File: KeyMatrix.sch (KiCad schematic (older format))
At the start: 104 parts, among them SW10 CherryMX, SW11 CherryMX, SW12 CherryMX, SW13 CherryMX, SW14 CherryMX, SW15 CherryMX, SW16 CherryMX, SW17 CherryMX, SW18 CherryMX, SW19 CherryMX, SW2 CherryMX, SW20 CherryMX, SW21 CherryMX, SW22 CherryMX, SW23 CherryMX, SW24 CherryMX, SW25 CherryMX, SW26 CherryMX, SW27 CherryMX, SW28 CherryMX, SW29 CherryMX, SW3 CherryMX, SW30 CherryMX, SW31 CherryMX, SW32 CherryMX, SW33 CherryMX, SW34 CherryMX, SW35 CherryMX, SW36 CherryMX, SW37 CherryMX, SW38 CherryMX, SW39 CherryMX, SW4 CherryMX, SW40 CherryMX, SW41 CherryMX, SW42 CherryMX, SW43 CherryMX, SW44 CherryMX, SW45 CherryMX, SW46 CherryMX, SW47 CherryMX, SW48 CherryMX, SW49 CherryMX, SW5 CherryMX, SW50 CherryMX, SW51 CherryMX, SW52 CherryMX, SW53 CherryMX, SW6 CherryMX, SW7 CherryMX, SW8 CherryMX, SW9 CherryMX

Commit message: Case outline and mounting
Received kprepublic case, used dimensions to set drawing of case and pcb outline. Created M2 screw footprint and added mounting holes to project. Tied screws to power gnd, will possibly change to signal ground later. Changed switches to be kailh hotswaps.
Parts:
- removed D52: D, ortho-40percent:SOD-123, symbol master-vampire_General:D
- removed SW53: CherryMX, CherryMX:SW_Cherry-MX_1U_PCB-Mount, symbol MKB_Switches:CherryMX
- SW10, SW11, SW12, SW13, SW14, SW15, SW16, SW17, SW18, SW19, SW2, SW20, SW21, SW22, SW23, SW24, SW25, SW26, SW27, SW28, SW29, SW3, SW30, SW31, SW32, SW33, SW34, SW35, SW36, SW37, SW38, SW39, SW4, SW40, SW41, SW42, SW43, SW44, SW45, SW46, SW47, SW48, SW49, SW5, SW6, SW7, SW8, SW9: footprint CherryMX:SW_Cherry-MX_1U_PCB-Mount -> CherryMX:SW_Cherry-MX_1U_PCB-Mount_Kailh-Hot-Swap
- SW50, SW51, SW52: footprint CherryMX:SW_Cherry-MX_1U_PCB-Mount -> CherryMX:SW_Cherry-MX_1U_PCB-Mount_Kailh-Hot-Swap; Package 1u -> 2u

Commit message: 2u footprint and plate comments
Finished 2u footprint in all styles. Added cutouts by using Cmts.User layer.
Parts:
- SW50, SW51, SW52: footprint CherryMX:SW_Cherry-MX_1U_PCB-Mount_Kailh-Hot-Swap -> CherryMX:SW_Cherry-MX_2U_PCB-Mount_Kailh-Hot-Swap
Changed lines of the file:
@@
 F 0 "SW50" H 8833 4955 50  0000 C CNN
 F 1 "CherryMX" H 8833 4864 50  0000 C CNN
-F 2 "CherryMX:SW_Cherry-MX_1U_PCB-Mount_Kailh-Hot-Swap" H 9600 4650 50  0001 C CNN
+F 2 "CherryMX:SW_Cherry-MX_2U_PCB-Mount_Kailh-Hot-Swap" H 9600 4650 50  0001 C CNN
 F 3 "" H 9500 4650 50  0001 C CNN
 F 4 "DNP" H 8700 4550 50  0001 C CNN "Manufacturer"
@@
 F 0 "SW51" H 8833 6155 50  0000 C CNN
 F 1 "CherryMX" H 8833 6064 50  0000 C CNN
-F 2 "CherryMX:SW_Cherry-MX_1U_PCB-Mount_Kailh-Hot-Swap" H 9600 5850 50  0001 C CNN
+F 2 "CherryMX:SW_Cherry-MX_2U_PCB-Mount_Kailh-Hot-Swap" H 9600 5850 50  0001 C CNN
 F 3 "" H 9500 5850 50  0001 C CNN
 F 4 "DNP" H 8700 5750 50  0001 C CNN "Manufacturer"
@@
 F 0 "SW52" H 8833 7355 50  0000 C CNN
 F 1 "CherryMX" H 8833 7264 50  0000 C CNN
-F 2 "CherryMX:SW_Cherry-MX_1U_PCB-Mount_Kailh-Hot-Swap" H 9600 7050 50  0001 C CNN
+F 2 "CherryMX:SW_Cherry-MX_2U_PCB-Mount_Kailh-Hot-Swap" H 9600 7050 50  0001 C CNN
 F 3 "" H 9500 7050 50  0001 C CNN
 F 4 "DNP" H 8700 6950 50  0001 C CNN "Manufacturer"

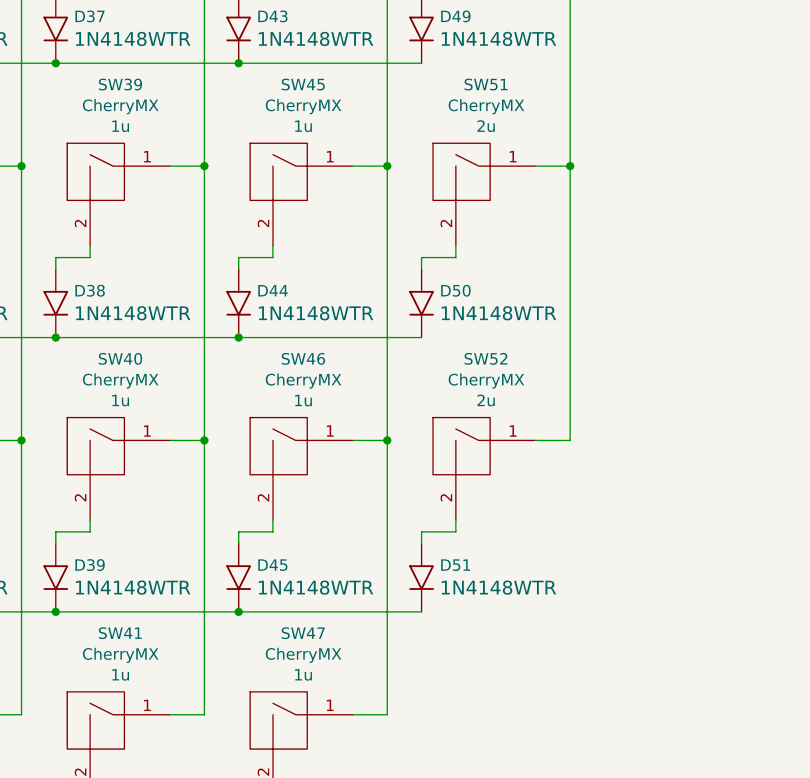
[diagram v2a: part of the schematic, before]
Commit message: Fixed case, pcb, screw locations
Set origin to hole on bottom-left switch, based all pcb and case dimensions on that hole. Relocated screws to new locations, now they are symmetrical with key positions.
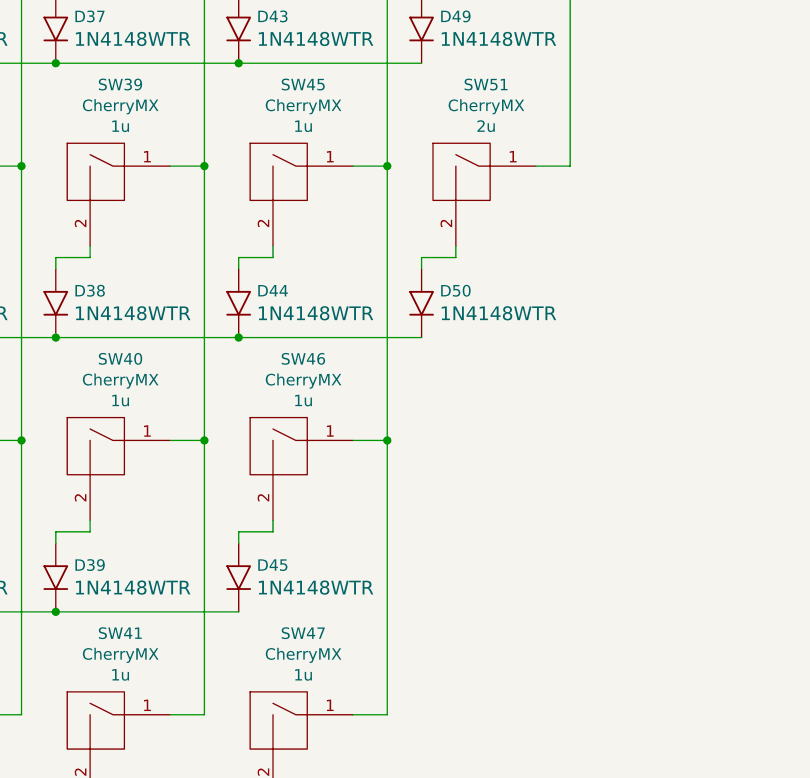
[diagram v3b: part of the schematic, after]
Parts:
- removed D51: D, ortho-40percent:SOD-123, symbol master-vampire_General:D
- removed SW52: CherryMX, CherryMX:SW_Cherry-MX_2U_PCB-Mount_Kailh-Hot-Swap, symbol MKB_Switches:CherryMX
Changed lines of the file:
@@
-$EndComp
-$Comp
-L MKB_Switches:CherryMX SW52
-U 1 1 5F52F49E
-P 8700 6950
-F 0 "SW52" H 8833 7355 50  0000 C CNN
-F 1 "CherryMX" H 8833 7264 50  0000 C CNN
-F 2 "CherryMX:SW_Cherry-MX_2U_PCB-Mount_Kailh-Hot-Swap" H 9600 7050 50  0001 C CNN
-F 3 "" H 9500 7050 50  0001 C CNN
-F 4 "DNP" H 8700 6950 50  0001 C CNN "Manufacturer"
-F 5 "DNP" H 8700 6950 50  0001 C CNN "MPN"
-F 6 "DNP" H 8700 6950 50  0001 C CNN "Supplier"
-F 7 "DNP" H 8700 6950 50  0001 C CNN "Supplier PN"
-F 8 "2u" H 8833 7173 50  0000 C CNN "Package"
-	1    8700 6950
-	1    0    0    -1
-$EndComp
-Wire Wire Line
-	9200 6900 9050 6900
-Wire Wire Line
-	8700 7250 8700 7300
-Wire Wire Line
-	8700 7300 8550 7300
-Wire Wire Line
-	8550 7300 8550 7350
-$Comp
-L master-vampire_General:D D51
-U 1 1 5F52F4B3
-P 8550 7500
-F 0 "D51" V 8603 7421 50  0000 R CNN
-F 1 "D" H 9000 7700 50  0001 C CNN
-F 2 "ortho-40percent:SOD-123" H 8450 7500 50  0001 C CNN
-F 3 "" H 8550 7600 50  0001 C CNN
-F 4 "1N4148WTR" V 8504 7421 60  0000 R CNN "MPN"
-F 5 "SMC Diode Solutions" H 9000 7800 60  0001 C CNN "Manufacturer"
-F 6 "DigiKey" H 8850 7900 50  0001 C CNN "Supplier"
-F 7 "1655-1360-1-ND" H 8950 8000 50  0001 C CNN "Supplier PN"
-F 8 "75V" V 8550 7421 50  0001 R CNN "Voltage Rating"
-F 9 "250mA" V 8459 7421 50  0001 R CNN "Current Rating"
-F 10 "SOD-123" H 9250 8300 50  0001 C CNN "Package"
-	1    8550 7500
-	0    -1   -1   0
 $EndComp
 $Comp
@@
 Wire Wire Line
 	9200 4500 9200 5700
-Connection ~ 9200 5700
-Wire Wire Line
-	9200 5700 9200 6900
 Wire Wire Line
 	2950 2850 3750 2850
@@
 Wire Wire Line
 	6950 7650 7750 7650
-Connection ~ 7750 7650
-Wire Wire Line
-	7750 7650 8550 7650
 Connection ~ 3750 8850
 Wire Wire Line

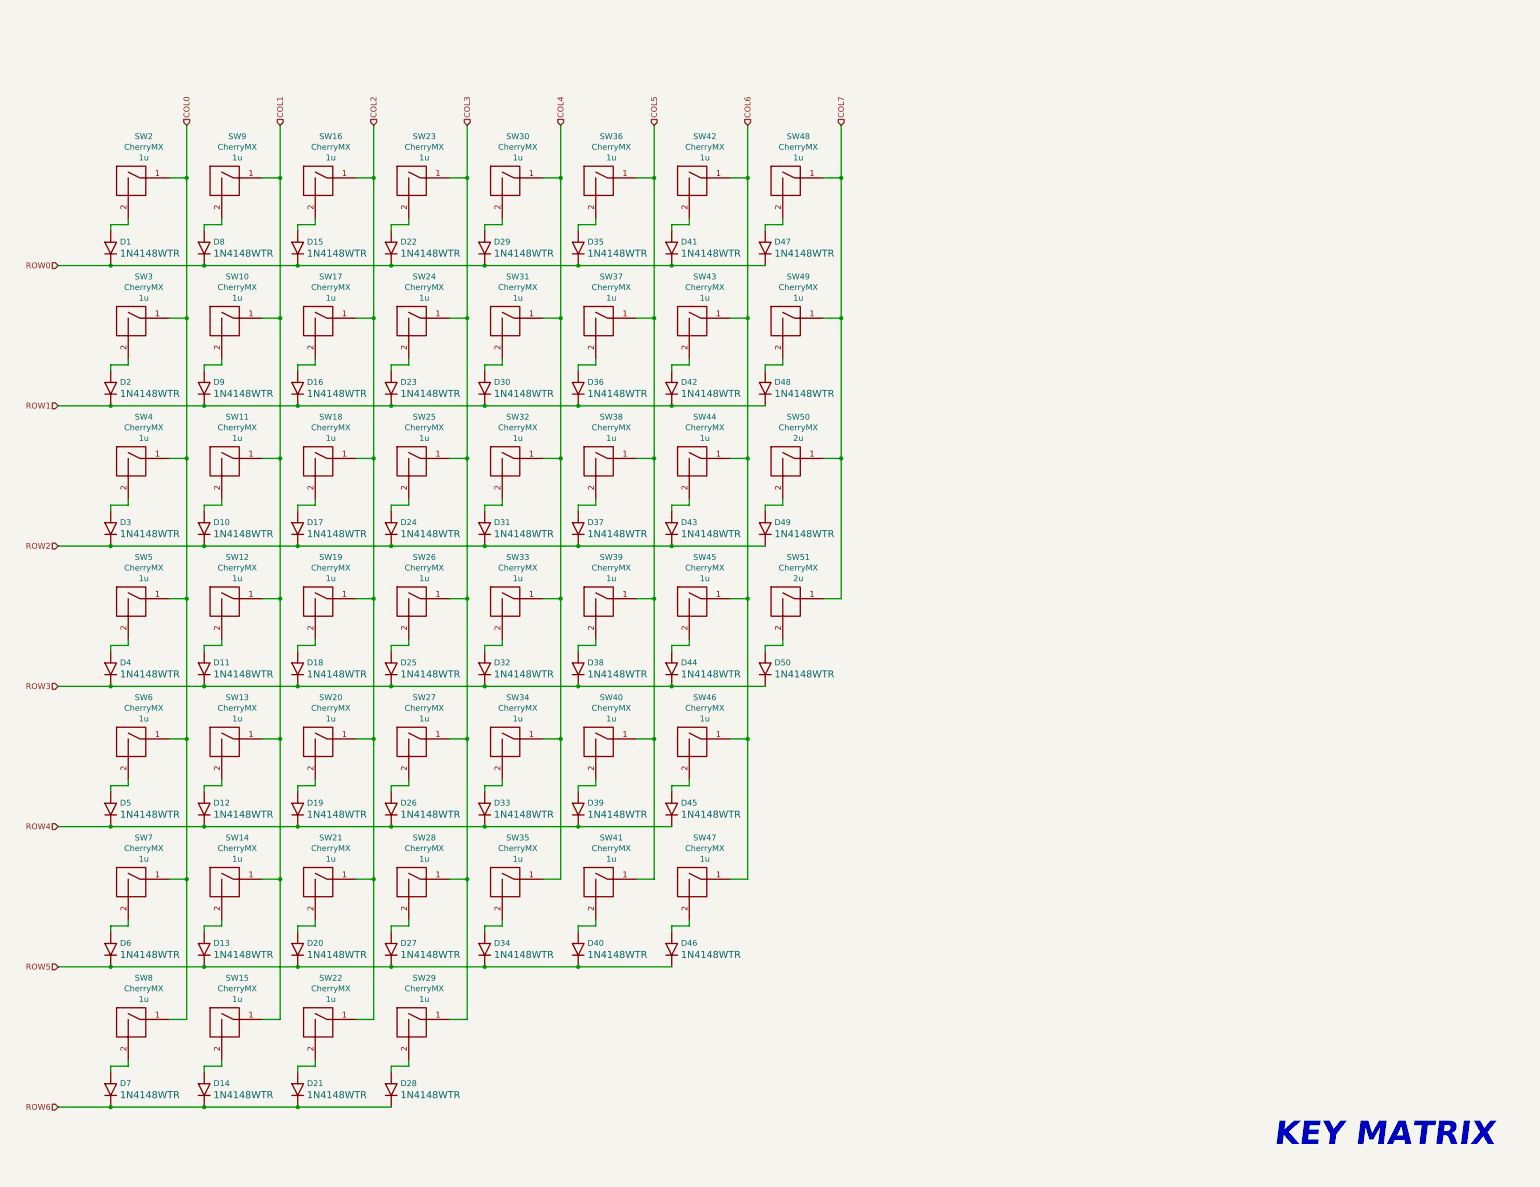
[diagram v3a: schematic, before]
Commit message: More key routing
Remapped keys to rows/columns to help optimize. Routed more.
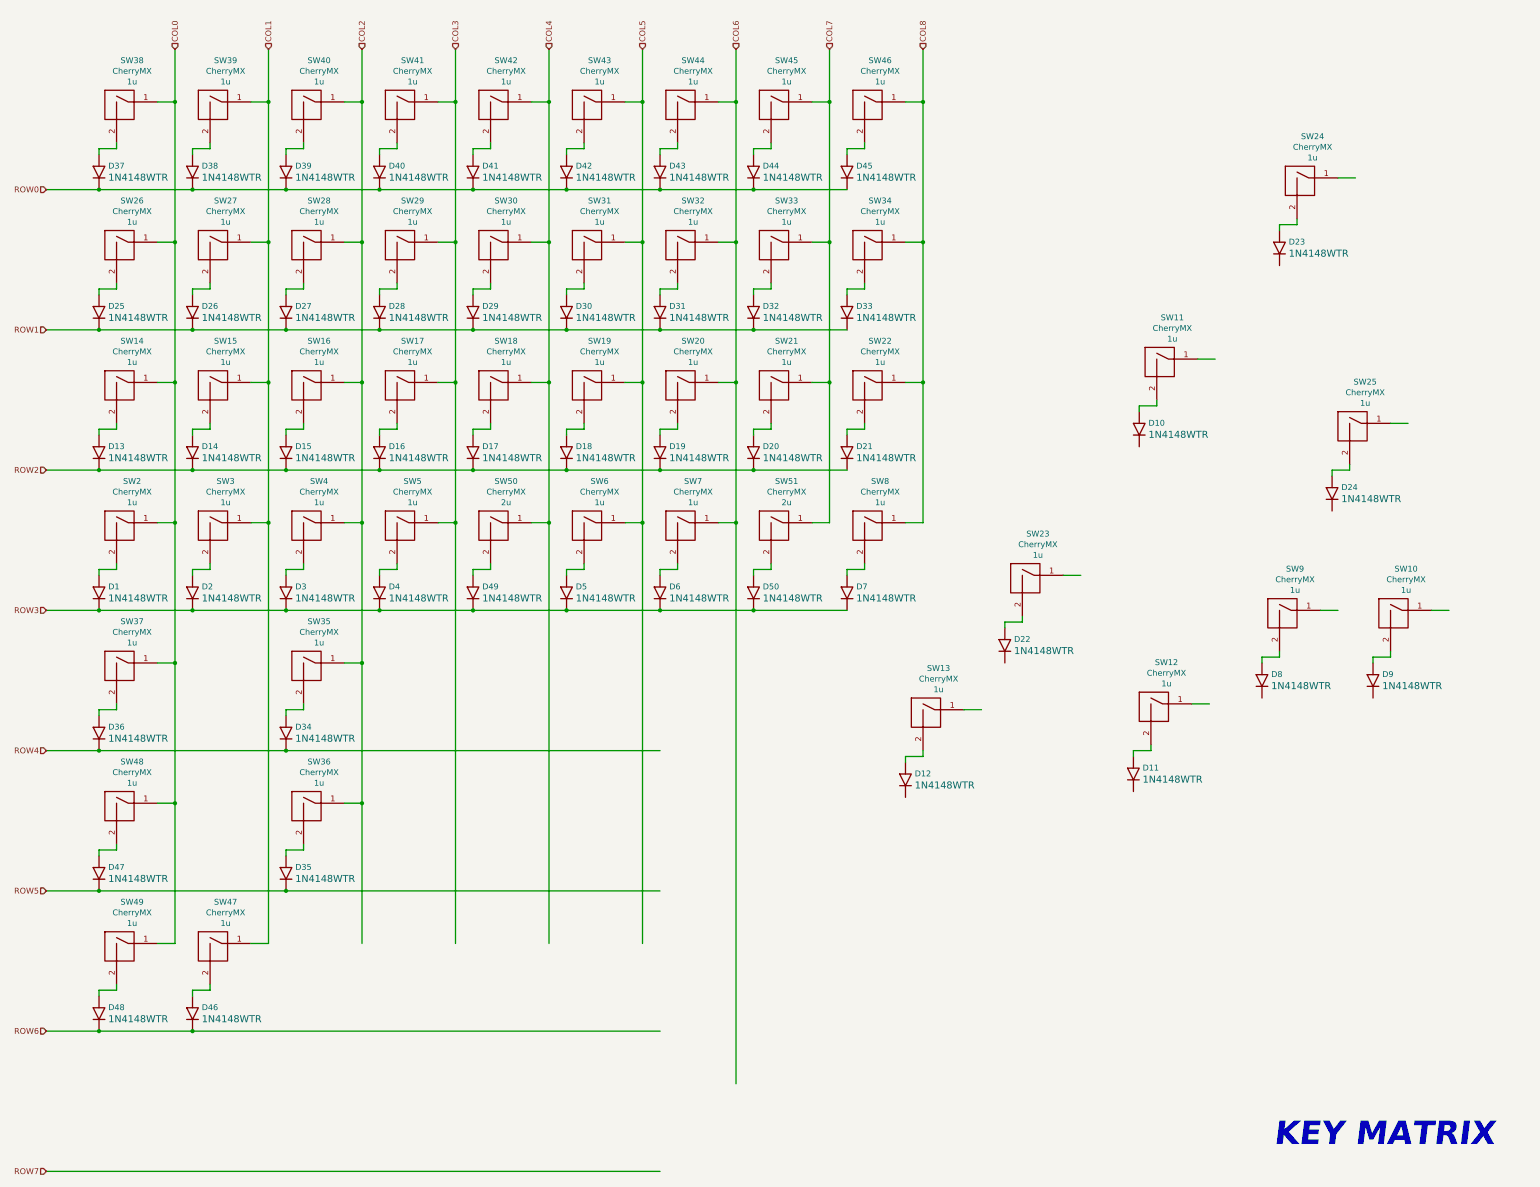
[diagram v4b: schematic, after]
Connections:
- net labels added: COL8, ROW7
- wire segments 300 -> 293
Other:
- moved on the sheet: D1, D10, D11, D12, D13, D14, D15, D16, D17, D18, D19, D2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

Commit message: More Routing
more routing
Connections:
- net labels added: COL10, COL9
- wire segments 293 -> 312
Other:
- moved on the sheet: D10, D11, D12, D22, D23, D24, D34, D35, D36, D46, D47, D48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

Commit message: more routing
more routing
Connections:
- wire segments 312 -> 310
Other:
- moved on the sheet: D35, D47, SW36, SW48
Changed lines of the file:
@@
 L MKB_Switches:CherryMX SW36
 U 1 1 5F4FA06B
-P 3000 7500
-F 0 "SW36" H 3133 7905 50  0000 C CNN
-F 1 "CherryMX" H 3133 7814 50  0000 C CNN
-F 2 "CherryMX:SW_Cherry-MX_1U_PCB-Mount_Kailh-Hot-Swap" H 3900 7600 50  0001 C CNN
-F 3 "" H 3800 7600 50  0001 C CNN
-F 4 "DNP" H 3000 7500 50  0001 C CNN "Manufacturer"
-F 5 "DNP" H 3000 7500 50  0001 C CNN "MPN"
-F 6 "DNP" H 3000 7500 50  0001 C CNN "Supplier"
-F 7 "DNP" H 3000 7500 50  0001 C CNN "Supplier PN"
-F 8 "1u" H 3133 7723 50  0000 C CNN "Package"
-	1    3000 7500
-	1    0    0    -1
-$EndComp
-Wire Wire Line
-	3500 7450 3350 7450
-Wire Wire Line
-	3000 7800 3000 7850
-Wire Wire Line
-	3000 7850 2850 7850
-Wire Wire Line
-	2850 7850 2850 7900
+P 11000 5100
+F 0 "SW36" H 11133 5505 50  0000 C CNN
+F 1 "CherryMX" H 11133 5414 50  0000 C CNN
+F 2 "CherryMX:SW_Cherry-MX_1U_PCB-Mount_Kailh-Hot-Swap" H 11900 5200 50  0001 C CNN
+F 3 "" H 11800 5200 50  0001 C CNN
+F 4 "DNP" H 11000 5100 50  0001 C CNN "Manufacturer"
+F 5 "DNP" H 11000 5100 50  0001 C CNN "MPN"
+F 6 "DNP" H 11000 5100 50  0001 C CNN "Supplier"
+F 7 "DNP" H 11000 5100 50  0001 C CNN "Supplier PN"
+F 8 "1u" H 11133 5323 50  0000 C CNN "Package"
+	1    11000 5100
+	1    0    0    -1
+$EndComp
+Wire Wire Line
+	11500 5050 11350 5050
+Wire Wire Line
+	11000 5400 11000 5450
+Wire Wire Line
+	11000 5450 10850 5450
+Wire Wire Line
+	10850 5450 10850 5500
 $Comp
 L master-vampire_General:D D35
 U 1 1 5F4FA080
-P 2850 8050
-F 0 "D35" V 2903 7971 50  0000 R CNN
-F 1 "D" H 3300 8250 50  0001 C CNN
-F 2 "ortho-40percent:SOD-123" H 2750 8050 50  0001 C CNN
-F 3 "" H 2850 8150 50  0001 C CNN
-F 4 "1N4148WTR" V 2804 7971 60  0000 R CNN "MPN"
-F 5 "SMC Diode Solutions" H 3300 8350 60  0001 C CNN "Manufacturer"
-F 6 "DigiKey" H 3150 8450 50  0001 C CNN "Supplier"
-F 7 "1655-1360-1-ND" H 3250 8550 50  0001 C CNN "Supplier PN"
-F 8 "75V" V 2850 7971 50  0001 R CNN "Voltage Rating"
-F 9 "250mA" V 2759 7971 50  0001 R CNN "Current Rating"
-F 10 "SOD-123" H 3550 8850 50  0001 C CNN "Package"
-	1    2850 8050
+P 10850 5650
+F 0 "D35" V 10903 5571 50  0000 R CNN
+F 1 "D" H 11300 5850 50  0001 C CNN
+F 2 "ortho-40percent:SOD-123" H 10750 5650 50  0001 C CNN
+F 3 "" H 10850 5750 50  0001 C CNN
+F 4 "1N4148WTR" V 10804 5571 60  0000 R CNN "MPN"
+F 5 "SMC Diode Solutions" H 11300 5950 60  0001 C CNN "Manufacturer"
+F 6 "DigiKey" H 11150 6050 50  0001 C CNN "Supplier"
+F 7 "1655-1360-1-ND" H 11250 6150 50  0001 C CNN "Supplier PN"
+F 8 "75V" V 10850 5571 50  0001 R CNN "Voltage Rating"
+F 9 "250mA" V 10759 5571 50  0001 R CNN "Current Rating"
+F 10 "SOD-123" H 11550 6450 50  0001 C CNN "Package"
+	1    10850 5650
 	0    -1   -1   0
 $EndComp
@@
 	6050 5800 6850 5800
 Connection ~ 6700 5050
-Wire Wire Line
-	2400 8200 2850 8200
-Connection ~ 2850 8200
-Connection ~ 3500 7450
-Wire Wire Line
-	3500 7450 3500 8650
 Connection ~ 9250 7000
 Connection ~ 8450 7000
 Wire Wire Line
 	8450 7000 9250 7000
-Wire Wire Line
-	3500 5050 3500 7450
 Wire Wire Line
 	9100 3850 9100 5050
@@
 Connection ~ 9900 6250
 Wire Wire Line
-	10050 5800 10400 5800
-Wire Wire Line
-	5250 8200 8450 8200
-Wire Wire Line
-	5900 5050 5900 7450
-Wire Wire Line
-	5900 7450 5900 8650
-Connection ~ 5900 7450
-Connection ~ 5250 8200
-Wire Wire Line
-	11500 1000 11500 6250
+	11500 1000 11500 3850
 $Comp
 L master-vampire_General:D D47
 U 1 1 5F4FA0C8
-P 5250 8050
-F 0 "D47" V 5303 7971 50  0000 R CNN
-F 1 "D" H 5700 8250 50  0001 C CNN
-F 2 "ortho-40percent:SOD-123" H 5150 8050 50  0001 C CNN
-F 3 "" H 5250 8150 50  0001 C CNN
-F 4 "1N4148WTR" V 5204 7971 60  0000 R CNN "MPN"
-F 5 "SMC Diode Solutions" H 5700 8350 60  0001 C CNN "Manufacturer"
-F 6 "DigiKey" H 5550 8450 50  0001 C CNN "Supplier"
-F 7 "1655-1360-1-ND" H 5650 8550 50  0001 C CNN "Supplier PN"
-F 8 "75V" V 5250 7971 50  0001 R CNN "Voltage Rating"
-F 9 "250mA" V 5159 7971 50  0001 R CNN "Current Rating"
-F 10 "SOD-123" H 5950 8850 50  0001 C CNN "Package"
-	1    5250 8050
-	0    -1   -1   0
-$EndComp
-Wire Wire Line
-	5250 7850 5250 7900
-Wire Wire Line
-	5400 7850 5250 7850
-Wire Wire Line
-	5400 7800 5400 7850
-Wire Wire Line
-	5900 7450 5750 7450
+P 10850 4450
+F 0 "D47" V 10903 4371 50  0000 R CNN
+F 1 "D" H 11300 4650 50  0001 C CNN
+F 2 "ortho-40percent:SOD-123" H 10750 4450 50  0001 C CNN
+F 3 "" H 10850 4550 50  0001 C CNN
+F 4 "1N4148WTR" V 10804 4371 60  0000 R CNN "MPN"
+F 5 "SMC Diode Solutions" H 11300 4750 60  0001 C CNN "Manufacturer"
+F 6 "DigiKey" H 11150 4850 50  0001 C CNN "Supplier"
+F 7 "1655-1360-1-ND" H 11250 4950 50  0001 C CNN "Supplier PN"
+F 8 "75V" V 10850 4371 50  0001 R CNN "Voltage Rating"
+F 9 "250mA" V 10759 4371 50  0001 R CNN "Current Rating"
+F 10 "SOD-123" H 11550 5250 50  0001 C CNN "Package"
+	1    10850 4450
+	0    -1   -1   0
+$EndComp
+Wire Wire Line
+	10850 4250 10850 4300
+Wire Wire Line
+	11000 4250 10850 4250
+Wire Wire Line
+	11000 4200 11000 4250
+Wire Wire Line
+	11500 3850 11350 3850
 $Comp
 L MKB_Switches:CherryMX SW48
 U 1 1 5F4FA0B3
-P 5400 7500
-F 0 "SW48" H 5533 7905 50  0000 C CNN
-F 1 "CherryMX" H 5533 7814 50  0000 C CNN
-F 2 "CherryMX:SW_Cherry-MX_1U_PCB-Mount_Kailh-Hot-Swap" H 6300 7600 50  0001 C CNN
-F 3 "" H 6200 7600 50  0001 C CNN
-F 4 "DNP" H 5400 7500 50  0001 C CNN "Manufacturer"
-F 5 "DNP" H 5400 7500 50  0001 C CNN "MPN"
-F 6 "DNP" H 5400 7500 50  0001 C CNN "Supplier"
-F 7 "DNP" H 5400 7500 50  0001 C CNN "Supplier PN"
-F 8 "1u" H 5533 7723 50  0000 C CNN "Package"
-	1    5400 7500
+P 11000 3900
+F 0 "SW48" H 11133 4305 50  0000 C CNN
+F 1 "CherryMX" H 11133 4214 50  0000 C CNN
+F 2 "CherryMX:SW_Cherry-MX_1U_PCB-Mount_Kailh-Hot-Swap" H 11900 4000 50  0001 C CNN
+F 3 "" H 11800 4000 50  0001 C CNN
+F 4 "DNP" H 11000 3900 50  0001 C CNN "Manufacturer"
+F 5 "DNP" H 11000 3900 50  0001 C CNN "MPN"
+F 6 "DNP" H 11000 3900 50  0001 C CNN "Supplier"
+F 7 "DNP" H 11000 3900 50  0001 C CNN "Supplier PN"
+F 8 "1u" H 11133 4123 50  0000 C CNN "Package"
+	1    11000 3900
 	1    0    0    -1
 $EndComp
@@
 Wire Wire Line
 	4300 5050 4300 8650
-Wire Wire Line
-	2850 8200 5250 8200
+Connection ~ 11500 5050
+Wire Wire Line
+	11500 5050 11500 6250
+Wire Wire Line
+	3500 5050 3500 8650
+Wire Wire Line
+	10050 5800 10850 5800
+Connection ~ 11500 3850
+Wire Wire Line
+	11500 3850 11500 5050
+Wire Wire Line
+	2400 8200 8450 8200
+Wire Wire Line
+	5900 5050 5900 8650
 $EndSCHEMATC

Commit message: More routing
even more routing
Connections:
- net labels removed: ROW6, ROW7
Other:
- moved on the sheet: D35, D47, SW36, SW48
